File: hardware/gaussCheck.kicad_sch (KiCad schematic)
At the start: 25 parts, among them J1 USB_C_Receptacle_USB2.0, SW2 PT847S, SW3 PT847S, SW4 PT847S, U1 TLV493D, U2 VIM-878-DP

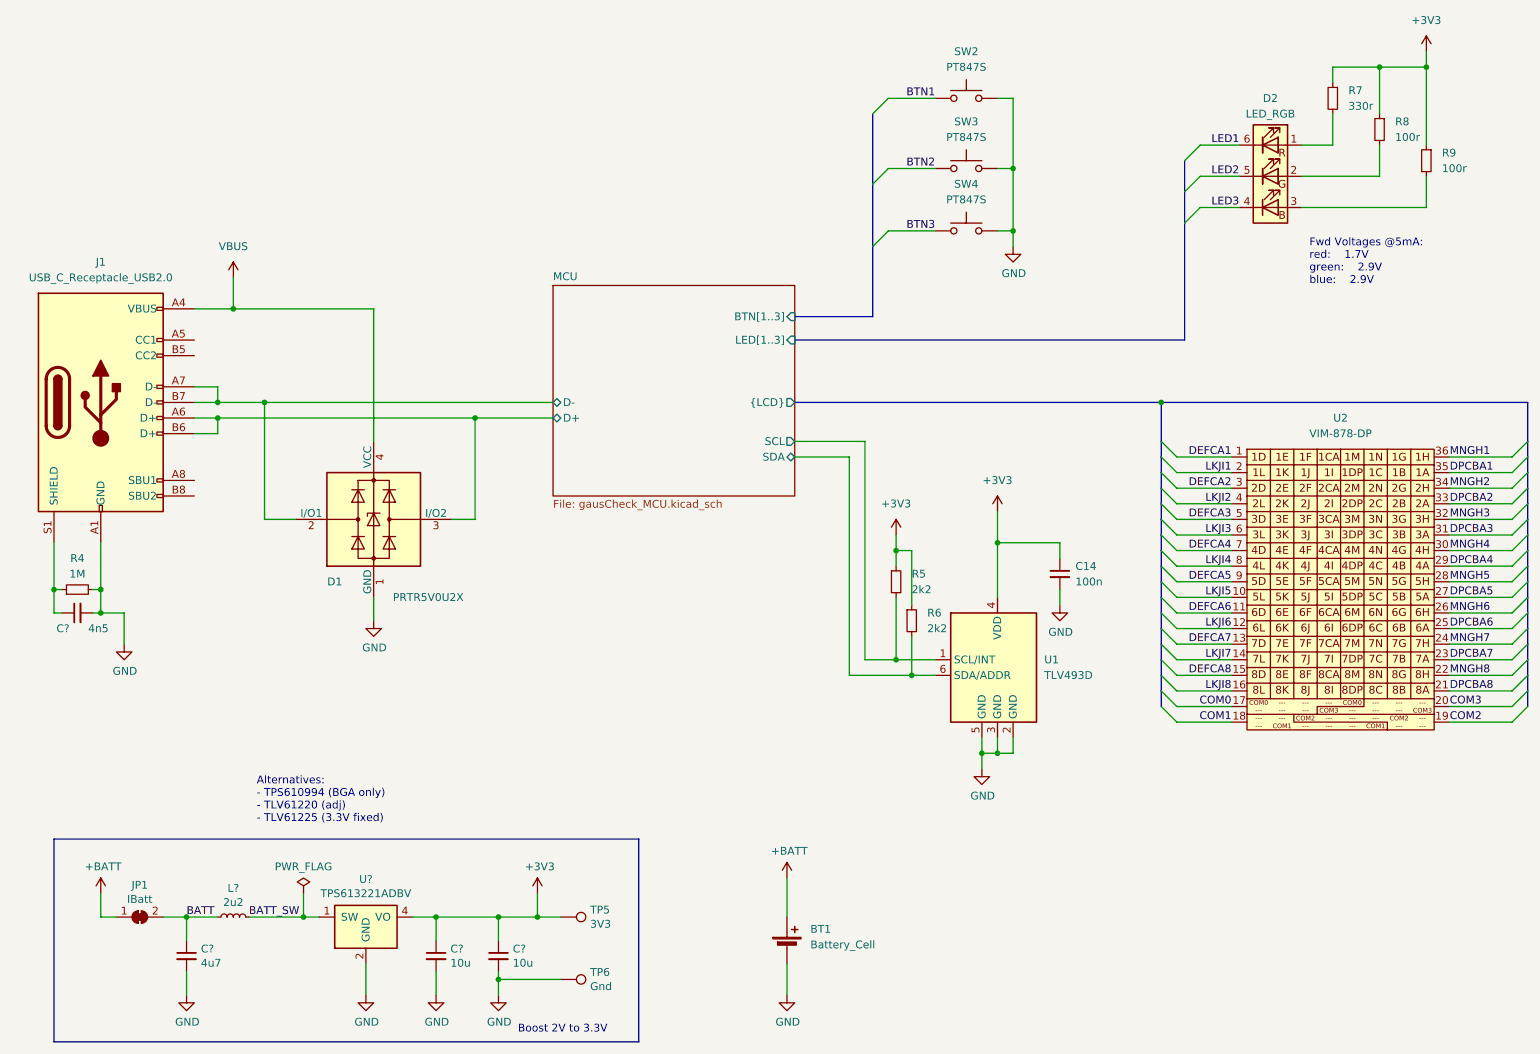
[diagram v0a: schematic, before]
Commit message: added 3V3 LDO added VBat Measurement
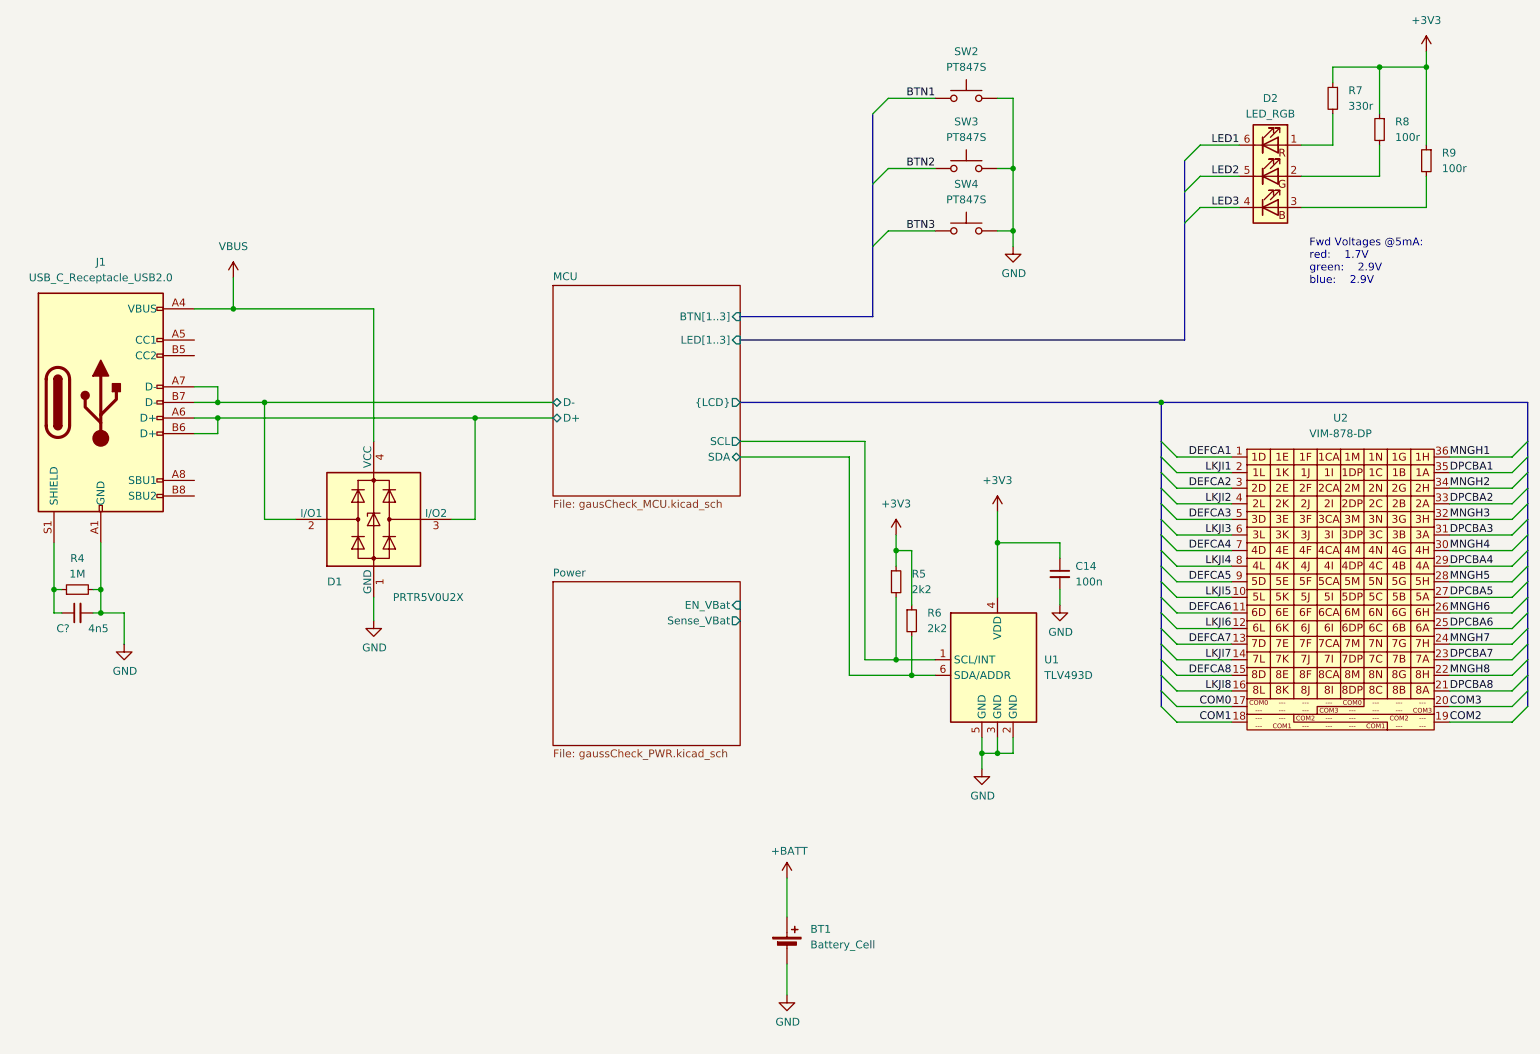
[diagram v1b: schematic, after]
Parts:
- removed C?: 4u7, Capacitor_SMD:C_0603_1608Metric, symbol Device:C_Small
- removed C? (x2): 10u, Capacitor_SMD:C_0603_1608Metric, symbol Device:C_Small
- removed JP1: IBatt, Jumper:SolderJumper-2_P1.3mm_Bridged_Pad1.0x1.5mm, symbol Jumper:SolderJumper_2_Bridged
- removed L?: 2u2, Knochi_Inductors:L_Murata_0806_2.00x1.60mm, symbol Device:L_Small
- removed TP5: 3V3, TestPoint:TestPoint_Pad_D1.5mm, symbol Connector:TestPoint
- removed TP6: Gnd, TestPoint:TestPoint_Pad_D1.5mm, symbol Connector:TestPoint
- removed U?: TPS613221ADBV, Package_TO_SOT_SMD:SOT-23-5, symbol SaniRemote-rescue:TPS613221ADBV-Knochi_Analog
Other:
- added sheet Power (gaussCheck_PWR.kicad_sch)
- note removed: "Alternatives: - TPS610994 (BGA only) - TLV61220 (adj) - TLV61225 (3.3V fixed)"
- note removed: "Boost 2V to 3.3V"

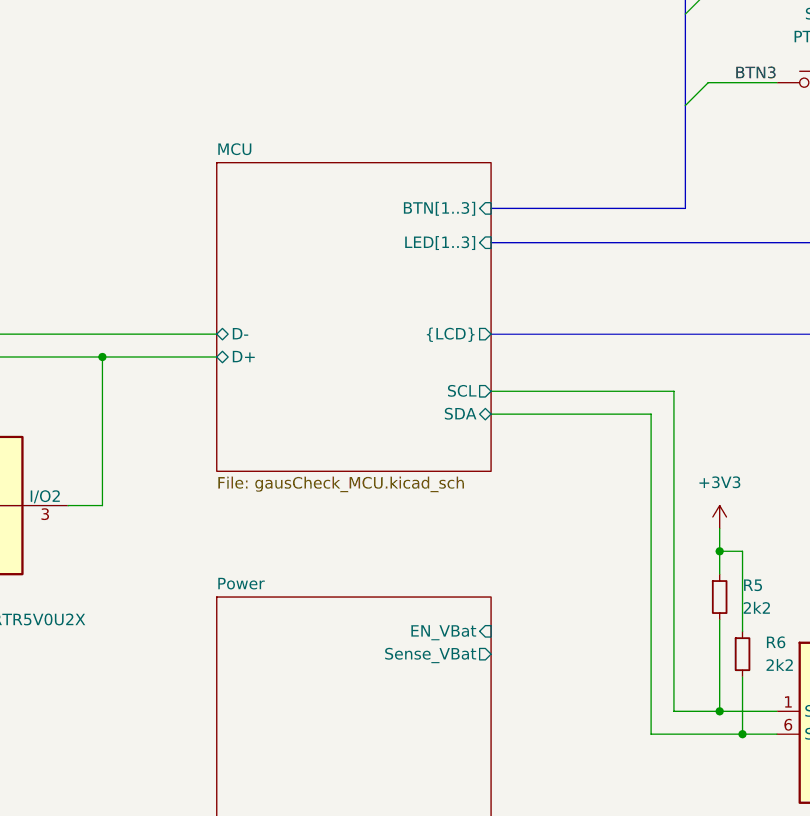
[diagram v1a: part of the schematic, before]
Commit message: added schottky diode to LDO connected en_vbat signal added a drawing of mems axis
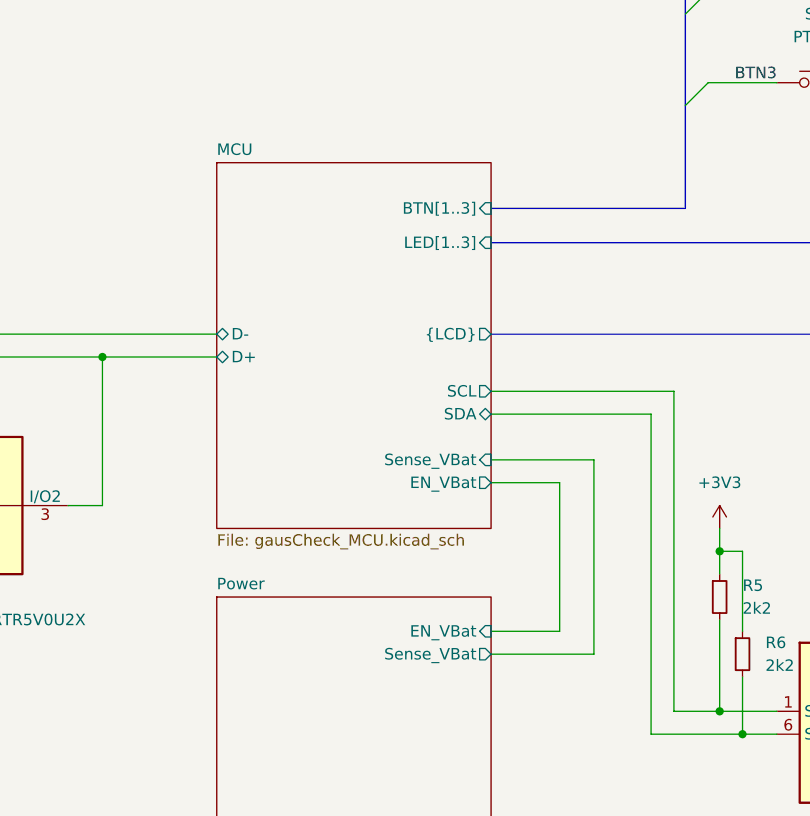
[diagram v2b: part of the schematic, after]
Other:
- sheet MCU ports: added EN_VBat, Sense_VBat; removed none
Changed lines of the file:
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@@
+    (stroke (width 0) (type default))
+  )
+  (wire (pts (xy 139.7 105.41) (xy 139.7 121.92))
     (stroke (width 0) (type default))
   )
@@
     (stroke (width 0) (type default))
   )
+  (wire (pts (xy 139.7 121.92) (xy 132.08 121.92))
+    (stroke (width 0) (type default))
+  )
   (wire (pts (xy 247.65 140.97) (xy 257.81 140.97))
     (stroke (width 0) (type default))
@@
     (stroke (width 0) (type default))
   )
+  (wire (pts (xy 132.08 105.41) (xy 139.7 105.41))
+    (stroke (width 0) (type default))
+  )
   (wire (pts (xy 171.45 143.51) (xy 171.45 146.05))
     (stroke (width 0) (type default))
@@
     (stroke (width 0) (type default))
   )
+  (wire (pts (xy 132.08 124.46) (xy 143.51 124.46))
+    (stroke (width 0) (type default))
+  )
   (wire (pts (xy 203.2 133.35) (xy 212.09 133.35))
     (stroke (width 0) (type default))
   )
   (wire (pts (xy 26.67 123.19) (xy 27.94 123.19))
+    (stroke (width 0) (type default))
+  )
+  (wire (pts (xy 143.51 124.46) (xy 143.51 102.87))
+    (stroke (width 0) (type default))
+  )
+  (wire (pts (xy 143.51 102.87) (xy 132.08 102.87))
     (stroke (width 0) (type default))
   )
@@
     )
   )
-  (sheet (at 101.6 69.85) (size 30.48 34.29) (fields_autoplaced)
+  (sheet (at 101.6 69.85) (size 30.48 40.64) (fields_autoplaced)
     (stroke (width 0.1524) (type solid))
     (fill (color 0 0 0 0.0000))
@@
       (effects (font (size 1.27 1.27)) (justify left bottom))
     )
-    (property "Sheetfile" "gausCheck_MCU.kicad_sch" (at 101.6 104.7246 0)
+    (property "Sheetfile" "gausCheck_MCU.kicad_sch" (at 101.6 111.0746 0)
       (effects (font (size 1.27 1.27)) (justify left top))
     )
@@
       (effects (font (size 1.27 1.27)) (justify right))
     )
+    (pin "Sense_VBat" input (at 132.08 102.87 0)
+      (effects (font (size 1.27 1.27)) (justify right))
+    )
+    (pin "EN_VBat" output (at 132.08 105.41 0)
+      (effects (font (size 1.27 1.27)) (justify right))
+    )

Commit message: updated some MPNs
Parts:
- D1: MPN (none) -> PRTR5V0U2X
- U1: MPN (none) -> TLV493D
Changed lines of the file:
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@@
+      (effects (font (size 1.27 1.27)) hide)
+    )
+    (property "MPN" "TLV493D" (at 173.99 133.35 0)
       (effects (font (size 1.27 1.27)) hide)
     )
@@
       (effects (font (size 1.27 1.27)) hide)
     )
+    (property "MPN" "PRTR5V0U2X" (at 72.39 107.95 0)
+      (effects (font (size 1.27 1.27)) hide)
+    )

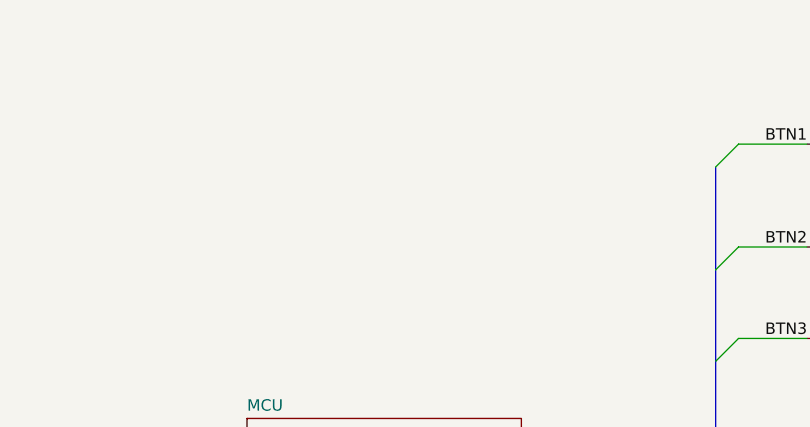
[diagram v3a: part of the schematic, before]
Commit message: added daughter board for LCD lightning
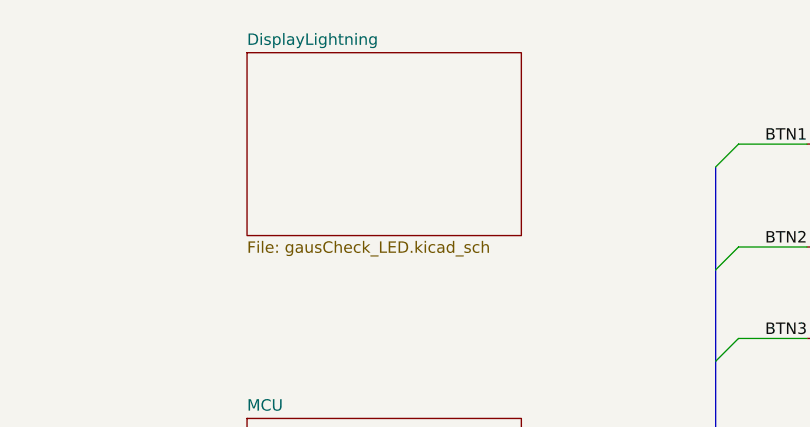
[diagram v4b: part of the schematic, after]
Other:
- added sheet DisplayLightning (gausCheck_LED.kicad_sch)
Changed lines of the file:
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@@
+    )
+  )
+  (sheet (at 101.6 29.21) (size 30.48 20.32) (fields_autoplaced)
+    (stroke (width 0.1524) (type solid))
+    (fill (color 0 0 0 0.0000))
+    (property "Sheetname" "DisplayLightning" (at 101.6 28.4984 0)
+      (effects (font (size 1.27 1.27)) (justify left bottom))
+    )
+    (property "Sheetfile" "gausCheck_LED.kicad_sch" (at 101.6 50.1146 0)
+      (effects (font (size 1.27 1.27)) (justify left top))
+    )
+    (instances
+      (project "gaussCheck"
+        (path "/cf3c710d-e38a-496a-b88d-8d225bc2685b" (page "4"))
+      )
     )
   )
